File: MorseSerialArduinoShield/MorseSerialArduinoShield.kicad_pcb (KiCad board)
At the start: 2 copper layers, 12 parts, among them U1 SC39-11SRWA

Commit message: startpoint
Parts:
- BZ1: footprint Buzzer_Beeper:Buzzer_15x7.5RM7.6 -> Buzzer_Beeper:Buzzer_12x9.5RM7.6
- moved R8 6.84 mm to (135.1, 88.3)
- moved RV1 6.35 mm to (127.5, 76.8)
- moved BZ1 6.35 mm to (145.3, 84.5), turned to 0 degrees
- moved R7 5.24 mm to (161.8, 111.1)
- moved R3 3.59 mm to (135.1, 95.9)
- moved R4 3.59 mm to (161.8, 88.3)
- moved R1 2.84 mm to (135.1, 111.1)
- moved R5 2.84 mm to (161.8, 95.9)
- moved R2 2.54 mm to (135.1, 103.5)
- moved R6 1.80 mm to (161.8, 103.5)
- moved U1 1.80 mm to (156.7, 106.0)

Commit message: fright hand rework
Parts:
- moved RV1 5.08 mm to (127.5, 81.9), turned to 180 degrees
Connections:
- R1 pad 2: Net-(A1-Pad20) -> Net-(A1-Pad26)
- R2 pad 2: Net-(A1-Pad17) -> Net-(A1-Pad25)
- R4 pad 2: Net-(A1-Pad26) -> Net-(A1-Pad17)
- R5 pad 2: Net-(A1-Pad25) -> Net-(A1-Pad19)
- R6 pad 2: Net-(A1-Pad19) -> Net-(A1-Pad20)
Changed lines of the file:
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@@
   )
   (module Potentiometer_THT:Potentiometer_Runtron_RM-065_Vertical (layer F.Cu)
-    (at 127.508 76.835)
+    (at 127.508 81.915 180)
     (descr "Potentiometer, vertical, Trimmer, RM-065 http://www.runtron.com/down/PDF%20Datasheet/Carbon%20Film%20Potentiometer/RM065%20RM063.pdf")
     (tags "Potentiometer Trimmer RM-065")
@@
     (fp_line (start -1.03 -1.55) (end 6.03 -1.55) (layer F.CrtYd) (width 0.05))
     (fp_circle (center 2.5 2.5) (end 5.5 2.5) (layer F.Fab) (width 0.1))
-    (fp_text user %R (at 2.5 2.5) (layer F.Fab)
+    (fp_text user %R (at 2.5 2.5 180) (layer F.Fab)
       (effects (font (size 1 1) (thickness 0.15)))
     )
@@
     (fp_line (start 5.71 -1.21) (end 5.81 -1.21) (layer F.SilkS) (width 0.12))
     (fp_line (start 5.81 -1.21) (end 5.81 -0.52) (layer F.SilkS) (width 0.12))
-    (pad 2 thru_hole circle (at 2.5 5) (size 1.55 1.55) (drill 1) (layers *.Cu *.Mask)
+    (pad 2 thru_hole circle (at 2.5 5 180) (size 1.55 1.55) (drill 1) (layers *.Cu *.Mask)
       (net 7 "Net-(A1-Pad28)"))
-    (pad 1 thru_hole rect (at 0 0) (size 1.55 1.55) (drill 1) (layers *.Cu *.Mask)
+    (pad 1 thru_hole rect (at 0 0 180) (size 1.55 1.55) (drill 1) (layers *.Cu *.Mask)
       (net 33 "Net-(BZ1-Pad1)"))
-    (pad 3 thru_hole circle (at 5 0) (size 1.55 1.55) (drill 1) (layers *.Cu *.Mask)
+    (pad 3 thru_hole circle (at 5 0 180) (size 1.55 1.55) (drill 1) (layers *.Cu *.Mask)
       (net 7 "Net-(A1-Pad28)"))
     (model ${KISYS3DMOD}/Potentiometer_THT.3dshapes/Potentiometer_Runtron_RM-065_Vertical.wrl
@@
     (fp_line (start 1.85 -1.6) (end 1.85 1.6) (layer F.Fab) (width 0.1))
     (pad 2 thru_hole oval (at 12.7 0) (size 1.6 1.6) (drill 0.8) (layers *.Cu *.Mask)
-      (net 25 "Net-(A1-Pad19)"))
+      (net 23 "Net-(A1-Pad20)"))
     (pad 1 thru_hole circle (at 0 0) (size 1.6 1.6) (drill 0.8) (layers *.Cu *.Mask)
       (net 39 "Net-(R6-Pad1)"))
@@
       (effects (font (size 1 1) (thickness 0.15)))
     )
-    (fp_text user %R (at 6.35 0) (layer F.Fab)
-      (effects (font (size 1 1) (thickness 0.15)))
-    )
-    (fp_line (start 13.75 -1.85) (end -1.05 -1.85) (layer F.CrtYd) (width 0.05))
-    (fp_line (start 13.75 1.85) (end 13.75 -1.85) (layer F.CrtYd) (width 0.05))
-    (fp_line (start -1.05 1.85) (end 13.75 1.85) (layer F.CrtYd) (width 0.05))
-    (fp_line (start -1.05 -1.85) (end -1.05 1.85) (layer F.CrtYd) (width 0.05))
-    (fp_line (start 11.66 0) (end 10.97 0) (layer F.SilkS) (width 0.12))
-    (fp_line (start 1.04 0) (end 1.73 0) (layer F.SilkS) (width 0.12))
-    (fp_line (start 10.97 -1.72) (end 1.73 -1.72) (layer F.SilkS) (width 0.12))
-    (fp_line (start 10.97 1.72) (end 10.97 -1.72) (layer F.SilkS) (width 0.12))
-    (fp_line (start 1.73 1.72) (end 10.97 1.72) (layer F.SilkS) (width 0.12))
-    (fp_line (start 1.73 -1.72) (end 1.73 1.72) (layer F.SilkS) (width 0.12))
-    (fp_line (start 12.7 0) (end 10.85 0) (layer F.Fab) (width 0.1))
-    (fp_line (start 0 0) (end 1.85 0) (layer F.Fab) (width 0.1))
-    (fp_line (start 10.85 -1.6) (end 1.85 -1.6) (layer F.Fab) (width 0.1))
-    (fp_line (start 10.85 1.6) (end 10.85 -1.6) (layer F.Fab) (width 0.1))
-    (fp_line (start 1.85 1.6) (end 10.85 1.6) (layer F.Fab) (width 0.1))
-    (fp_line (start 1.85 -1.6) (end 1.85 1.6) (layer F.Fab) (width 0.1))
-    (pad 2 thru_hole oval (at 12.7 0) (size 1.6 1.6) (drill 0.8) (layers *.Cu *.Mask)
-      (net 13 "Net-(A1-Pad25)"))
+    (fp_line (start 1.85 -1.6) (end 1.85 1.6) (layer F.Fab) (width 0.1))
+    (fp_line (start 1.85 1.6) (end 10.85 1.6) (layer F.Fab) (width 0.1))
+    (fp_line (start 10.85 1.6) (end 10.85 -1.6) (layer F.Fab) (width 0.1))
+    (fp_line (start 10.85 -1.6) (end 1.85 -1.6) (layer F.Fab) (width 0.1))
+    (fp_line (start 0 0) (end 1.85 0) (layer F.Fab) (width 0.1))
+    (fp_line (start 12.7 0) (end 10.85 0) (layer F.Fab) (width 0.1))
+    (fp_line (start 1.73 -1.72) (end 1.73 1.72) (layer F.SilkS) (width 0.12))
+    (fp_line (start 1.73 1.72) (end 10.97 1.72) (layer F.SilkS) (width 0.12))
+    (fp_line (start 10.97 1.72) (end 10.97 -1.72) (layer F.SilkS) (width 0.12))
+    (fp_line (start 10.97 -1.72) (end 1.73 -1.72) (layer F.SilkS) (width 0.12))
+    (fp_line (start 1.04 0) (end 1.73 0) (layer F.SilkS) (width 0.12))
+    (fp_line (start 11.66 0) (end 10.97 0) (layer F.SilkS) (width 0.12))
+    (fp_line (start -1.05 -1.85) (end -1.05 1.85) (layer F.CrtYd) (width 0.05))
+    (fp_line (start -1.05 1.85) (end 13.75 1.85) (layer F.CrtYd) (width 0.05))
+    (fp_line (start 13.75 1.85) (end 13.75 -1.85) (layer F.CrtYd) (width 0.05))
+    (fp_line (start 13.75 -1.85) (end -1.05 -1.85) (layer F.CrtYd) (width 0.05))
+    (fp_text user %R (at 6.35 0) (layer F.Fab)
+      (effects (font (size 1 1) (thickness 0.15)))
+    )
     (pad 1 thru_hole circle (at 0 0) (size 1.6 1.6) (drill 0.8) (layers *.Cu *.Mask)
       (net 38 "Net-(R5-Pad1)"))
+    (pad 2 thru_hole oval (at 12.7 0) (size 1.6 1.6) (drill 0.8) (layers *.Cu *.Mask)
+      (net 25 "Net-(A1-Pad19)"))
     (model ${KISYS3DMOD}/Resistor_THT.3dshapes/R_Axial_DIN0309_L9.0mm_D3.2mm_P12.70mm_Horizontal.wrl
       (at (xyz 0 0 0))
@@
     (fp_line (start 1.85 -1.6) (end 1.85 1.6) (layer F.Fab) (width 0.1))
     (pad 2 thru_hole oval (at 12.7 0) (size 1.6 1.6) (drill 0.8) (layers *.Cu *.Mask)
-      (net 11 "Net-(A1-Pad26)"))
+      (net 29 "Net-(A1-Pad17)"))
     (pad 1 thru_hole circle (at 0 0) (size 1.6 1.6) (drill 0.8) (layers *.Cu *.Mask)
       (net 37 "Net-(R4-Pad1)"))
@@
       (effects (font (size 1 1) (thickness 0.15)))
     )
-    (fp_text user %R (at 6.35 0) (layer F.Fab)
-      (effects (font (size 1 1) (thickness 0.15)))
-    )
-    (fp_line (start 13.75 -1.85) (end -1.05 -1.85) (layer F.CrtYd) (width 0.05))
-    (fp_line (start 13.75 1.85) (end 13.75 -1.85) (layer F.CrtYd) (width 0.05))
-    (fp_line (start -1.05 1.85) (end 13.75 1.85) (layer F.CrtYd) (width 0.05))
-    (fp_line (start -1.05 -1.85) (end -1.05 1.85) (layer F.CrtYd) (width 0.05))
-    (fp_line (start 11.66 0) (end 10.97 0) (layer F.SilkS) (width 0.12))
-    (fp_line (start 1.04 0) (end 1.73 0) (layer F.SilkS) (width 0.12))
-    (fp_line (start 10.97 -1.72) (end 1.73 -1.72) (layer F.SilkS) (width 0.12))
-    (fp_line (start 10.97 1.72) (end 10.97 -1.72) (layer F.SilkS) (width 0.12))
-    (fp_line (start 1.73 1.72) (end 10.97 1.72) (layer F.SilkS) (width 0.12))
-    (fp_line (start 1.73 -1.72) (end 1.73 1.72) (layer F.SilkS) (width 0.12))
-    (fp_line (start 12.7 0) (end 10.85 0) (layer F.Fab) (width 0.1))
-    (fp_line (start 0 0) (end 1.85 0) (layer F.Fab) (width 0.1))
-    (fp_line (start 10.85 -1.6) (end 1.85 -1.6) (layer F.Fab) (width 0.1))
-    (fp_line (start 10.85 1.6) (end 10.85 -1.6) (layer F.Fab) (width 0.1))
-    (fp_line (start 1.85 1.6) (end 10.85 1.6) (layer F.Fab) (width 0.1))
-    (fp_line (start 1.85 -1.6) (end 1.85 1.6) (layer F.Fab) (width 0.1))
-    (pad 2 thru_hole oval (at 12.7 0 180) (size 1.6 1.6) (drill 0.8) (layers *.Cu *.Mask)
-      (net 29 "Net-(A1-Pad17)"))
+    (fp_line (start 1.85 -1.6) (end 1.85 1.6) (layer F.Fab) (width 0.1))
+    (fp_line (start 1.85 1.6) (end 10.85 1.6) (layer F.Fab) (width 0.1))
+    (fp_line (start 10.85 1.6) (end 10.85 -1.6) (layer F.Fab) (width 0.1))
+    (fp_line (start 10.85 -1.6) (end 1.85 -1.6) (layer F.Fab) (width 0.1))
+    (fp_line (start 0 0) (end 1.85 0) (layer F.Fab) (width 0.1))
+    (fp_line (start 12.7 0) (end 10.85 0) (layer F.Fab) (width 0.1))
+    (fp_line (start 1.73 -1.72) (end 1.73 1.72) (layer F.SilkS) (width 0.12))
+    (fp_line (start 1.73 1.72) (end 10.97 1.72) (layer F.SilkS) (width 0.12))
+    (fp_line (start 10.97 1.72) (end 10.97 -1.72) (layer F.SilkS) (width 0.12))
+    (fp_line (start 10.97 -1.72) (end 1.73 -1.72) (layer F.SilkS) (width 0.12))
+    (fp_line (start 1.04 0) (end 1.73 0) (layer F.SilkS) (width 0.12))
+    (fp_line (start 11.66 0) (end 10.97 0) (layer F.SilkS) (width 0.12))
+    (fp_line (start -1.05 -1.85) (end -1.05 1.85) (layer F.CrtYd) (width 0.05))
+    (fp_line (start -1.05 1.85) (end 13.75 1.85) (layer F.CrtYd) (width 0.05))
+    (fp_line (start 13.75 1.85) (end 13.75 -1.85) (layer F.CrtYd) (width 0.05))
+    (fp_line (start 13.75 -1.85) (end -1.05 -1.85) (layer F.CrtYd) (width 0.05))
+    (fp_text user %R (at 6.35 0) (layer F.Fab)
+      (effects (font (size 1 1) (thickness 0.15)))
+    )
     (pad 1 thru_hole circle (at 0 0 180) (size 1.6 1.6) (drill 0.8) (layers *.Cu *.Mask)
       (net 35 "Net-(R2-Pad1)"))
+    (pad 2 thru_hole oval (at 12.7 0 180) (size 1.6 1.6) (drill 0.8) (layers *.Cu *.Mask)
+      (net 13 "Net-(A1-Pad25)"))
     (model ${KISYS3DMOD}/Resistor_THT.3dshapes/R_Axial_DIN0309_L9.0mm_D3.2mm_P12.70mm_Horizontal.wrl
       (at (xyz 0 0 0))
@@
     (fp_line (start 1.85 -1.6) (end 1.85 1.6) (layer F.Fab) (width 0.1))
     (pad 2 thru_hole oval (at 12.7 0 180) (size 1.6 1.6) (drill 0.8) (layers *.Cu *.Mask)
-      (net 23 "Net-(A1-Pad20)"))
+      (net 11 "Net-(A1-Pad26)"))
     (pad 1 thru_hole circle (at 0 0 180) (size 1.6 1.6) (drill 0.8) (layers *.Cu *.Mask)
       (net 34 "Net-(R1-Pad1)"))

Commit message: done design
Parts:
- moved R6 1.80 mm to (160.5, 104.8)
- moved R4 1.80 mm to (160.5, 89.5)
- moved R5 1.80 mm to (160.5, 97.2)
- moved R7 1.80 mm to (160.5, 112.4)
- moved U1 1.27 mm to (155.4, 106.0)
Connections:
- R1 pad 2: Net-(A1-Pad26) -> Net-(A1-Pad22)
- R2 pad 2: Net-(A1-Pad25) -> Net-(A1-Pad23)
- R3 pad 2: Net-(A1-Pad23) -> Net-(A1-Pad25)
- R6 pad 2: Net-(A1-Pad20) -> Net-(A1-Pad21)
- R7 pad 2: Net-(A1-Pad21) -> Net-(A1-Pad20)
- R8 pad 2: Net-(A1-Pad22) -> Net-(A1-Pad26)
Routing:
- net Net-(A1-Pad28): track 0.00 -> 84.9 mm
- net Net-(A1-Pad26): track 0.00 -> 66.2 mm
- net GND: track 0.00 -> 57.7 mm
- net Net-(A1-Pad25): track 0.00 -> 57.1 mm
- net Net-(A1-Pad23): track 0.00 -> 57.0 mm
- net Net-(A1-Pad17): track 0.00 -> 46.8 mm
- net Net-(A1-Pad22): track 0.00 -> 46.2 mm
- net Net-(A1-Pad19): track 0.00 -> 39.5 mm
- net Net-(A1-Pad21): track 0.00 -> 24.8 mm
- net Net-(BZ1-Pad1): track 0.00 -> 18.8 mm
- net Net-(A1-Pad20): track 0.00 -> 16.2 mm
- net Net-(R8-Pad1): track 0.00 -> 10.6 mm
- net Net-(R7-Pad1): track 0.00 -> 9.34 mm
- net Net-(R4-Pad1): track 0.00 -> 8.45 mm
- net Net-(R1-Pad1): track 0.00 -> 7.18 mm
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
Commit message: latest changes
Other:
- board outline added: 77.5 x 58.4 mm
- board text added: "Arduino Morse Code Beep and Display Version 1.0"
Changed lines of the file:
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@@
   (general
     (thickness 1.6)
-    (drawings 0)
+    (drawings 5)
     (tracks 79)
     (zones 0)
@@
     (visible_elements 7FFFFFFF)
     (pcbplotparams
-      (layerselection 0x00030_80000001)
+      (layerselection 0x010f0_ffffffff)
       (usegerberextensions false)
       (usegerberattributes false)
@@
       (outputformat 1)
       (mirror false)
-      (drillshape 1)
+      (drillshape 0)
       (scaleselection 1)
-      (outputdirectory ""))
+      (outputdirectory "Gerber/"))
   )
   (net 0 "")
@@
     )
   )
+  (gr_line (start 180.848 70.485) (end 180.848 128.905) (layer Edge.Cuts) (width 0.1))
+  (gr_line (start 103.378 70.485) (end 180.848 70.485) (layer Edge.Cuts) (width 0.1))
+  (gr_line (start 103.378 128.905) (end 103.378 70.485) (layer Edge.Cuts) (width 0.1))
+  (gr_line (start 180.848 128.905) (end 103.378 128.905) (layer Edge.Cuts) (width 0.1))
+  (gr_text "Arduino Morse Code\nBeep and Display\nVersion 1.0" (at 165.608 81.915) (layer F.SilkS)
+    (effects (font (size 1 1) (thickness 0.15)))
+  )
   (segment (start 152.888 84.455) (end 155.448 84.455) (width 0.25) (layer B.Cu) (net 1))

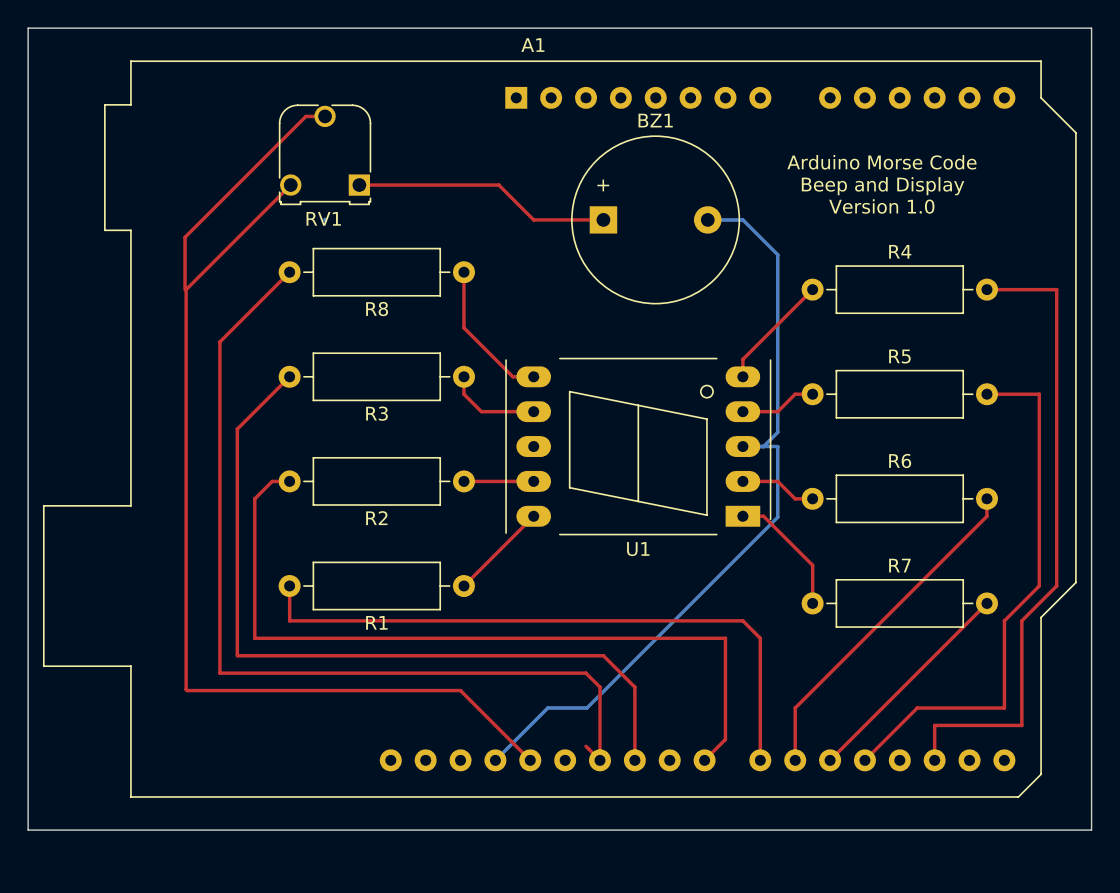
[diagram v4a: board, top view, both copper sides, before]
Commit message: kicad layout fix
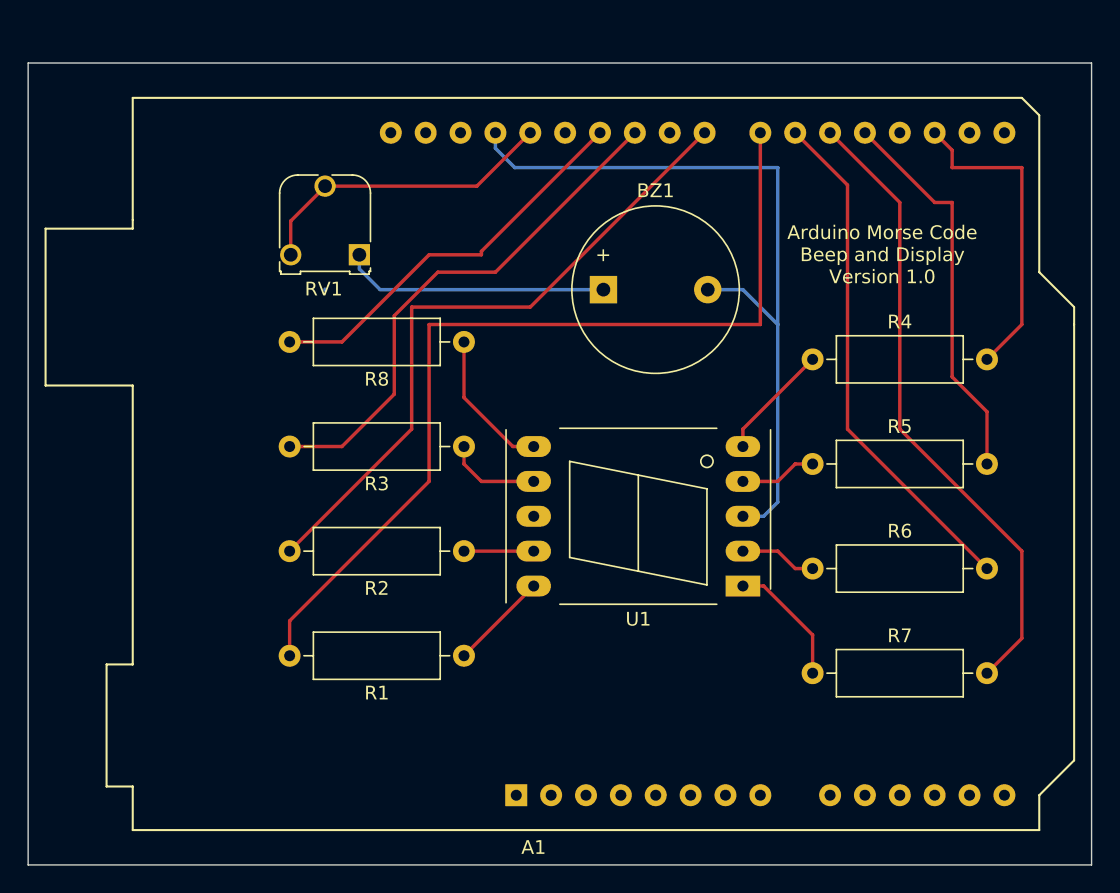
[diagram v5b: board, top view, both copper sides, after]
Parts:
- A1: moved to B.Cu
- moved A1 50.8 mm to (138.9, 126.4)
- moved BZ1 5.08 mm to (145.3, 89.5)
- moved R1 5.08 mm to (135.1, 116.2)
- moved R2 5.08 mm to (135.1, 108.6)
- moved R3 5.08 mm to (135.1, 101.0)
- moved R4 5.08 mm to (160.5, 94.6)
- moved R5 5.08 mm to (160.5, 102.2)
- moved R6 5.08 mm to (160.5, 109.9)
- moved R7 5.08 mm to (160.5, 117.5)
- moved R8 5.08 mm to (135.1, 93.3)
- moved RV1 5.08 mm to (127.5, 87.0)
- moved U1 5.08 mm to (155.4, 111.1)
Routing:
- net Net-(A1-Pad28): track 84.9 -> 22.7 mm
- net Net-(A1-Pad26): track 66.2 -> 29.1 mm
- net Net-(A1-Pad20): track 16.2 -> 46.2 mm
- net Net-(A1-Pad17): track 46.8 -> 23.2 mm
- net Net-(A1-Pad22): track 46.2 -> 66.4 mm
- net Net-(A1-Pad25): track 57.1 -> 38.0 mm
- net Net-(A1-Pad21): track 24.8 -> 37.5 mm
- net Net-(A1-Pad19): track 39.5 -> 28.6 mm
- net Net-(A1-Pad23): track 57.0 -> 48.1 mm
- net GND: track 57.7 -> 55.8 mm
- net Net-(BZ1-Pad1): track 18.8 -> 19.4 mm
